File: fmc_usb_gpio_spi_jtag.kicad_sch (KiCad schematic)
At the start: 10 parts

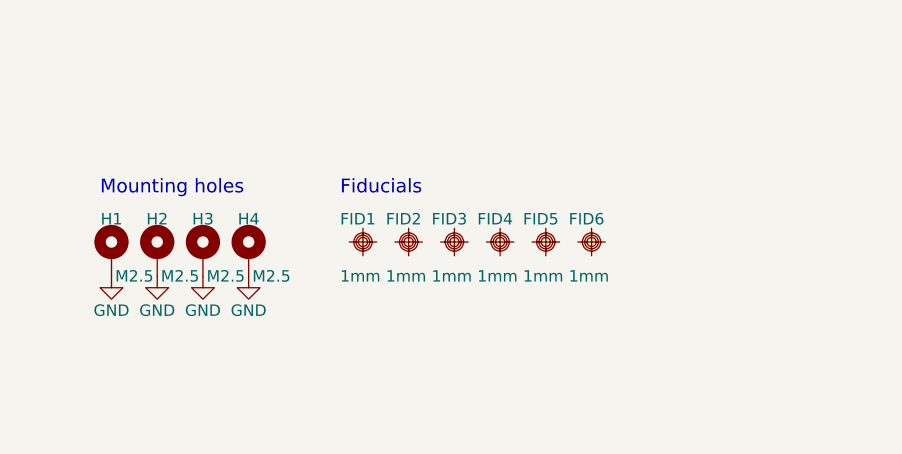
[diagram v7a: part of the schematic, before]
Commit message: *.kicad_sch: add notes about mechanical holes
Signed-off-by: Huang Rui <vowstar@gmail.com>
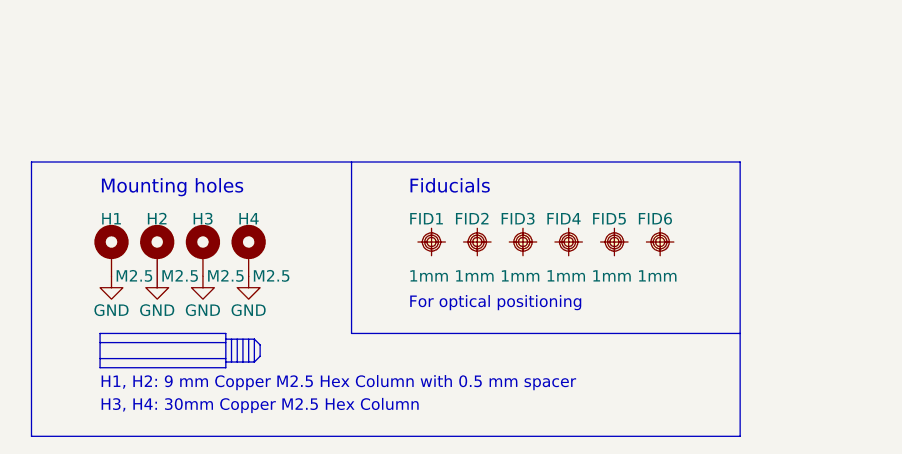
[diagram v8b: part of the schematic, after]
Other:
- note added: "For optical positioning"
- note added: "H1, H2: 9 mm Copper M2.5 Hex Column with 0.5 mm spacer"
- note added: "H3, H4: 30mm Copper M2.5 Hex Column"
- moved on the sheet: FID1, FID2, FID3, FID4, FID5, FID6
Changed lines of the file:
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@@
   )
   (bus_alias "USB_FS" (members "DET" "CON" "~{OE}" "RCV" "VP" "VM" "SPD" "SUS"))
+  (polyline (pts (xy 58.42 186.944) (xy 72.39 186.944))
+    (stroke (width 0) (type default))
+  )
+  (polyline (pts (xy 72.39 187.325) (xy 75.565 187.325))
+    (stroke (width 0) (type default))
+  )
+  (polyline (pts (xy 75.565 184.785) (xy 75.565 187.325))
+    (stroke (width 0) (type default))
+  )
+  (polyline (pts (xy 73.66 184.785) (xy 73.66 187.325))
+    (stroke (width 0) (type default))
+  )
+  (polyline (pts (xy 75.565 184.785) (xy 76.2 185.42))
+    (stroke (width 0) (type default))
+  )
+  (polyline (pts (xy 86.36 184.15) (xy 129.54 184.15))
+    (stroke (width 0) (type default))
+  )
+  (polyline (pts (xy 72.39 184.785) (xy 75.565 184.785))
+    (stroke (width 0) (type default))
+  )
+  (polyline (pts (xy 58.42 187.96) (xy 72.39 187.96))
+    (stroke (width 0) (type default))
+  )
+  (polyline (pts (xy 74.93 184.785) (xy 74.93 187.325))
+    (stroke (width 0) (type default))
+  )
+  (polyline (pts (xy 58.42 184.15) (xy 72.39 184.15))
+    (stroke (width 0) (type default))
+  )
+  (polyline (pts (xy 72.39 184.15) (xy 72.39 187.96))
+    (stroke (width 0) (type default))
+  )
   (bus (pts (xy 60.96 78.74) (xy 60.96 100.33))
     (stroke (width 0) (type default))
   )
+  (polyline (pts (xy 75.565 187.325) (xy 76.2 186.69))
+    (stroke (width 0) (type default))
+  )
+  (polyline (pts (xy 58.42 185.166) (xy 72.39 185.166))
+    (stroke (width 0) (type default))
+  )
+  (polyline (pts (xy 74.295 184.785) (xy 74.295 187.325))
+    (stroke (width 0) (type default))
+  )
+  (polyline (pts (xy 73.025 184.785) (xy 73.025 187.325))
+    (stroke (width 0) (type default))
+  )
+  (polyline (pts (xy 76.2 185.42) (xy 76.2 186.69))
+    (stroke (width 0) (type default))
+  )
+  (polyline (pts (xy 58.42 184.15) (xy 58.42 187.96))
+    (stroke (width 0) (type default))
+  )
   (bus (pts (xy 109.22 78.74) (xy 109.22 100.33))
     (stroke (width 0) (type default))
   )
-  (text "Fiducials" (at 85.09 168.91 0)
+  (polyline (pts (xy 86.36 165.1) (xy 86.36 184.15))
+    (stroke (width 0) (type default))
+  )
+  (rectangle (start 50.8 165.1) (end 129.54 195.58)
+    (stroke (width 0) (type default))
+    (fill (type none))
+  )
+  (text "H1, H2: 9 mm Copper M2.5 Hex Column with 0.5 mm spacer"
+    (at 58.42 190.5 0)
+    (effects (font (size 1.27 1.27)) (justify left bottom))
+  )
+  (text "For optical positioning" (at 92.71 181.61 0)
+    (effects (font (size 1.27 1.27)) (justify left bottom))
+  )
+  (text "Fiducials" (at 92.71 168.91 0)
     (effects (font (size 1.524 1.524)) (justify left bottom))
+  )
+  (text "H3, H4: 30mm Copper M2.5 Hex Column" (at 58.42 193.04 0)
+    (effects (font (size 1.27 1.27)) (justify left bottom))
   )
   (text "Mounting holes" (at 58.42 168.91 0)
@@
     )
   )
-  (symbol (lib_id "CHIPSAlliance_Mechanical:Fiducial") (at 97.79 173.99 0) (unit 1)
-    (in_bom yes) (on_board yes) (dnp no)
-    (property "Reference" "FID3" (at 95.25 171.45 0)
-      (effects (font (size 1.27 1.27)) (justify left))
-    )
-    (property "Value" "1mm" (at 95.25 177.8 0)
-      (effects (font (size 1.27 1.27)) (justify left))
-    )
-    (property "Footprint" "Fiducial:Fiducial_1mm_Mask2mm" (at 97.536 173.99 0)
-      (effects (font (size 1.27 1.27)) hide)
-    )
-    (property "Datasheet" "~" (at 97.79 173.99 0)
+  (symbol (lib_id "CHIPSAlliance_Mechanical:Fiducial") (at 105.41 173.99 0) (unit 1)
+    (in_bom yes) (on_board yes) (dnp no)
+    (property "Reference" "FID3" (at 102.87 171.45 0)
+      (effects (font (size 1.27 1.27)) (justify left))
+    )
+    (property "Value" "1mm" (at 102.87 177.8 0)
+      (effects (font (size 1.27 1.27)) (justify left))
+    )
+    (property "Footprint" "Fiducial:Fiducial_1mm_Mask2mm" (at 105.156 173.99 0)
+      (effects (font (size 1.27 1.27)) hide)
+    )
+    (property "Datasheet" "~" (at 105.41 173.99 0)
       (effects (font (size 1.27 1.27)) hide)
     )
@@
     )
   )
-  (symbol (lib_id "CHIPSAlliance_Mechanical:Fiducial") (at 113.03 173.99 0) (unit 1)
-    (in_bom yes) (on_board yes) (dnp no)
-    (property "Reference" "FID6" (at 110.49 171.45 0)
-      (effects (font (size 1.27 1.27)) (justify left))
-    )
-    (property "Value" "1mm" (at 110.49 177.8 0)
-      (effects (font (size 1.27 1.27)) (justify left))
-    )
-    (property "Footprint" "Fiducial:Fiducial_1mm_Mask2mm" (at 112.776 173.99 0)
-      (effects (font (size 1.27 1.27)) hide)
-    )
-    (property "Datasheet" "~" (at 113.03 173.99 0)
+  (symbol (lib_id "CHIPSAlliance_Mechanical:Fiducial") (at 120.65 173.99 0) (unit 1)
+    (in_bom yes) (on_board yes) (dnp no)
+    (property "Reference" "FID6" (at 118.11 171.45 0)
+      (effects (font (size 1.27 1.27)) (justify left))
+    )
+    (property "Value" "1mm" (at 118.11 177.8 0)
+      (effects (font (size 1.27 1.27)) (justify left))
+    )
+    (property "Footprint" "Fiducial:Fiducial_1mm_Mask2mm" (at 120.396 173.99 0)
+      (effects (font (size 1.27 1.27)) hide)
+    )
+    (property "Datasheet" "~" (at 120.65 173.99 0)
       (effects (font (size 1.27 1.27)) hide)
     )
@@
     )
   )
-  (symbol (lib_id "CHIPSAlliance_Mechanical:Fiducial") (at 107.95 173.99 0) (unit 1)
-    (in_bom yes) (on_board yes) (dnp no)
-    (property "Reference" "FID5" (at 105.41 171.45 0)
-      (effects (font (size 1.27 1.27)) (justify left))
-    )
-    (property "Value" "1mm" (at 105.41 177.8 0)
-      (effects (font (size 1.27 1.27)) (justify left))
-    )
-    (property "Footprint" "Fiducial:Fiducial_1mm_Mask2mm" (at 107.696 173.99 0)
-      (effects (font (size 1.27 1.27)) hide)
-    )
-    (property "Datasheet" "~" (at 107.95 173.99 0)
+  (symbol (lib_id "CHIPSAlliance_Mechanical:Fiducial") (at 115.57 173.99 0) (unit 1)
+    (in_bom yes) (on_board yes) (dnp no)
+    (property "Reference" "FID5" (at 113.03 171.45 0)
+      (effects (font (size 1.27 1.27)) (justify left))
+    )
+    (property "Value" "1mm" (at 113.03 177.8 0)
+      (effects (font (size 1.27 1.27)) (justify left))
+    )
+    (property "Footprint" "Fiducial:Fiducial_1mm_Mask2mm" (at 115.316 173.99 0)
+      (effects (font (size 1.27 1.27)) hide)
+    )
+    (property "Datasheet" "~" (at 115.57 173.99 0)
       (effects (font (size 1.27 1.27)) hide)
     )
@@
     )
   )
-  (symbol (lib_id "CHIPSAlliance_Mechanical:Fiducial") (at 102.87 173.99 0) (unit 1)
-    (in_bom yes) (on_board yes) (dnp no)
-    (property "Reference" "FID4" (at 100.33 171.45 0)
-      (effects (font (size 1.27 1.27)) (justify left))
-    )
-    (property "Value" "1mm" (at 100.33 177.8 0)
-      (effects (font (size 1.27 1.27)) (justify left))
-    )
-    (property "Footprint" "Fiducial:Fiducial_1mm_Mask2mm" (at 102.616 173.99 0)
-      (effects (font (size 1.27 1.27)) hide)
-    )
-    (property "Datasheet" "~" (at 102.87 173.99 0)
+  (symbol (lib_id "CHIPSAlliance_Mechanical:Fiducial") (at 110.49 173.99 0) (unit 1)
+    (in_bom yes) (on_board yes) (dnp no)
+    (property "Reference" "FID4" (at 107.95 171.45 0)
+      (effects (font (size 1.27 1.27)) (justify left))
+    )
+    (property "Value" "1mm" (at 107.95 177.8 0)
+      (effects (font (size 1.27 1.27)) (justify left))
+    )
+    (property "Footprint" "Fiducial:Fiducial_1mm_Mask2mm" (at 110.236 173.99 0)
+      (effects (font (size 1.27 1.27)) hide)
+    )
+    (property "Datasheet" "~" (at 110.49 173.99 0)
       (effects (font (size 1.27 1.27)) hide)
     )
@@
     )
   )
-  (symbol (lib_id "CHIPSAlliance_Mechanical:Fiducial") (at 92.71 173.99 0) (unit 1)
-    (in_bom yes) (on_board yes) (dnp no)
-    (property "Reference" "FID2" (at 90.17 171.45 0)
-      (effects (font (size 1.27 1.27)) (justify left))
-    )
-    (property "Value" "1mm" (at 90.17 177.8 0)
-      (effects (font (size 1.27 1.27)) (justify left))
-    )
-    (property "Footprint" "Fiducial:Fiducial_1mm_Mask2mm" (at 92.456 173.99 0)
-      (effects (font (size 1.27 1.27)) hide)
-    )
-    (property "Datasheet" "~" (at 92.71 173.99 0)
+  (symbol (lib_id "CHIPSAlliance_Mechanical:Fiducial") (at 100.33 173.99 0) (unit 1)
+    (in_bom yes) (on_board yes) (dnp no)
+    (property "Reference" "FID2" (at 97.79 171.45 0)
+      (effects (font (size 1.27 1.27)) (justify left))
+    )
+    (property "Value" "1mm" (at 97.79 177.8 0)
+      (effects (font (size 1.27 1.27)) (justify left))
+    )
+    (property "Footprint" "Fiducial:Fiducial_1mm_Mask2mm" (at 100.076 173.99 0)
+      (effects (font (size 1.27 1.27)) hide)
+    )
+    (property "Datasheet" "~" (at 100.33 173.99 0)
       (effects (font (size 1.27 1.27)) hide)
     )
@@
     )
   )
-  (symbol (lib_id "CHIPSAlliance_Mechanical:Fiducial") (at 87.63 173.99 0) (unit 1)
-    (in_bom yes) (on_board yes) (dnp no)
-    (property "Reference" "FID1" (at 85.09 171.45 0)
-      (effects (font (size 1.27 1.27)) (justify left))
-    )
-    (property "Value" "1mm" (at 85.09 177.8 0)
-      (effects (font (size 1.27 1.27)) (justify left))
-    )
-    (property "Footprint" "Fiducial:Fiducial_1mm_Mask2mm" (at 87.376 173.99 0)
-      (effects (font (size 1.27 1.27)) hide)
-    )
-    (property "Datasheet" "~" (at 87.63 173.99 0)
-      (effects (font (size 1.27 1.27)) hide)
-    )
+  (symbol (lib_id "CHIPSAlliance_Mechanical:Fiducial") (at 95.25 173.99 0) (unit 1)
+    (in_bom yes) (on_board yes) (dnp no)
+    (property "Reference" "FID1" (at 92.71 171.45 0)
+      (effects (font (size 1.27 1.27)) (justify left))
+    )
+    (property "Value" "1mm" (at 92.71 177.8 0)
+      (effects (font (size 1.27 1.27)) (justify left))
+    )
+    (property "Footprint" "Fiducial:Fiducial_1mm_Mask2mm" (at 94.996 173.99 0)
+      (effects (font (size 1.27 1.27)) hide)
+    )
+    (property "Datasheet" "~" (at 95.25 173.99 0)
+      (effects (font (size 1.27 1.27)) hide)
+    )
